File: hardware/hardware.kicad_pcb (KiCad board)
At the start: 2 copper layers, 91.4 x 91.4 mm, 104 parts, among them J1 DB25_Female, J2 USB_B_Micro, J3 RJ45_Bel_SI-60062-F-68net, J4 Conn_01x02_Male, J5 Conn_01x02_Male, U1 MIC5319, U11 ENC28J60x-SO, U12 74LVC14, U2 74LVTH126, U3 74LVTH126, U4 LM1117-ADJ, U5 74LVTH126, U6 74LVTH126, U7 STM32F072R8Tx, U8 74LVC245, Y1 8MHz, Y2 25MHz

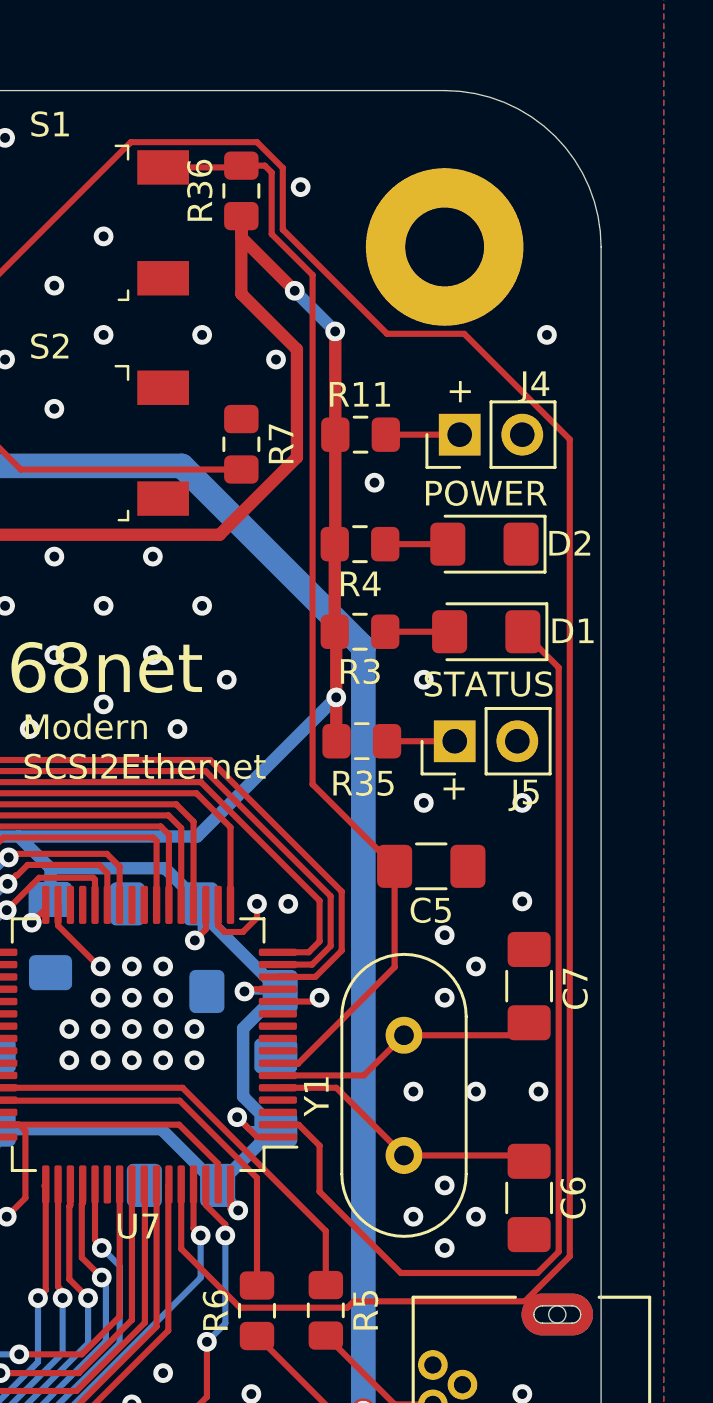
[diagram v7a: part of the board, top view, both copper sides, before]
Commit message: fix: wrong pins on LEDs connectors
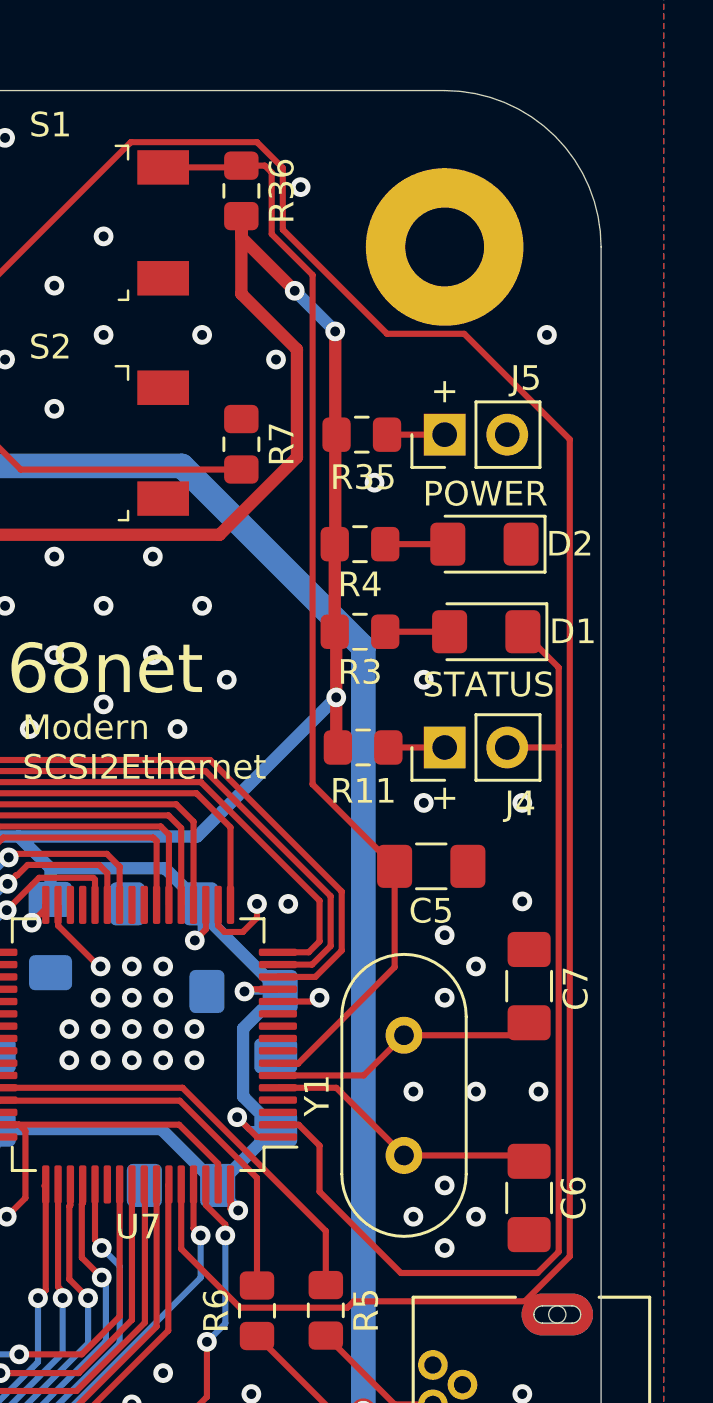
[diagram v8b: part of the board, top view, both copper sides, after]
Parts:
- moved J4 12.7 mm to (105.4, 47.0)
- moved R11 12.7 mm to (102.1, 47.0)
- moved J5 12.5 mm to (105.4, 34.3)
- moved R35 12.4 mm to (102.0, 34.3)
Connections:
- J4 pad 2: GND -> /STATUS_LED
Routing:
- net /STATUS_LED: track 41.1 -> 43.2 mm
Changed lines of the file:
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@@
     (thickness 1.6)
     (drawings 18)
-    (tracks 1581)
+    (tracks 1585)
     (zones 0)
     (modules 104)
@@
   )
   (setup
-    (last_trace_width 0.5)
+    (last_trace_width 0.25)
     (user_trace_width 0.25)
     (user_trace_width 0.5)
@@
     (tags "resistor handsolder")
     (attr smd)
-    (fp_text reference R36 (at 0 -1.65 90) (layer F.SilkS)
+    (fp_text reference R36 (at 0 1.651 90) (layer F.SilkS)
       (effects (font (size 1 1) (thickness 0.15)))
     )
@@
   )
   (module Resistor_SMD:R_0805_2012Metric_Pad1.15x1.40mm_HandSolder (layer F.Cu)
-    (at 102.045 46.736 180)
+    (at 102.045 34.29 180)
     (descr "Resistor SMD 0805 (2012 Metric), square (rectangular) end terminal, IPC_7351 nominal with elongated pad for handsoldering. (Body size source: https://docs.google.com/spreadsheets/d/1BsfQQcO9C6DZCsRaXUlFlo91Tg2WpOkGARC1WS5S8t0/edit?usp=sharing), generated with kicad-footprint-generator")
     (tags "resistor handsolder")
@@
   )
   (module Resistor_SMD:R_0805_2012Metric_Pad1.15x1.40mm_HandSolder (layer F.Cu)
-    (at 101.995 34.29 180)
+    (at 102.099 46.99 180)
     (descr "Resistor SMD 0805 (2012 Metric), square (rectangular) end terminal, IPC_7351 nominal with elongated pad for handsoldering. (Body size source: https://docs.google.com/spreadsheets/d/1BsfQQcO9C6DZCsRaXUlFlo91Tg2WpOkGARC1WS5S8t0/edit?usp=sharing), generated with kicad-footprint-generator")
     (tags "resistor handsolder")
     (attr smd)
-    (fp_text reference R11 (at 0.025 1.6) (layer F.SilkS)
+    (fp_text reference R11 (at -0.009 -1.778) (layer F.SilkS)
       (effects (font (size 1 1) (thickness 0.15)))
     )
@@
   )
   (module Connector_PinHeader_2.54mm:PinHeader_1x02_P2.54mm_Vertical (layer F.Cu)
-    (at 105.82 46.736 90)
+    (at 105.41 34.29 90)
     (descr "Through hole straight pin header, 1x02, 2.54mm pitch, single row")
     (tags "Through hole pin header THT 1x02 2.54mm single row")
-    (fp_text reference J5 (at -2.1 2.892 180) (layer F.SilkS)
+    (fp_text reference J5 (at 2.286 3.302 180) (layer F.SilkS)
       (effects (font (size 1 1) (thickness 0.15)))
     )
@@
   )
   (module Connector_PinHeader_2.54mm:PinHeader_1x02_P2.54mm_Vertical (layer F.Cu)
-    (at 106.02 34.29 90)
+    (at 105.41 46.99 90)
     (descr "Through hole straight pin header, 1x02, 2.54mm pitch, single row")
     (tags "Through hole pin header THT 1x02 2.54mm single row")
-    (fp_text reference J4 (at 2.032 3.073 180) (layer F.SilkS)
+    (fp_text reference J4 (at -2.286 3.073 180) (layer F.SilkS)
       (effects (font (size 1 1) (thickness 0.15)))
     )
@@
     )
     (pad 2 thru_hole oval (at 0 2.54 90) (size 1.7 1.7) (drill 1) (layers *.Cu *.Mask)
-      (net 1 GND))
+      (net 15 /STATUS_LED))
     (pad 1 thru_hole rect (at 0 0 90) (size 1.7 1.7) (drill 1) (layers *.Cu *.Mask)
       (net 111 "Net-(J4-Pad1)"))
@@
     )
   )
-  (gr_text + (at 106.045 32.512) (layer F.SilkS)
+  (gr_text + (at 105.41 32.512) (layer F.SilkS)
     (effects (font (size 1 1) (thickness 0.2)))
   )
-  (gr_text + (at 105.791 48.641) (layer F.SilkS)
+  (gr_text + (at 105.41 49.022) (layer F.SilkS)
     (effects (font (size 1 1) (thickness 0.2)))
   )
@@
   (segment (start 100.33 63.155298) (end 100.33 65.024) (width 0.25) (layer F.Cu) (net 15))
   (segment (start 100.33 65.024) (end 103.632 68.326) (width 0.25) (layer F.Cu) (net 15))
-  (segment (start 110.03901 67.46618) (end 110.03901 43.74501) (width 0.25) (layer F.Cu) (net 15))
   (segment (start 110.03901 43.74501) (end 108.585 42.291) (width 0.25) (layer F.Cu) (net 15))
   (segment (start 109.17919 68.326) (end 110.03901 67.46618) (width 0.25) (layer F.Cu) (net 15))
   (segment (start 103.632 68.326) (end 109.17919 68.326) (width 0.25) (layer F.Cu) (net 15))
+  (segment (start 107.95 46.99) (end 109.982 46.99) (width 0.25) (layer F.Cu) (net 15))
+  (segment (start 110.03901 46.93299) (end 110.03901 43.74501) (width 0.25) (layer F.Cu) (net 15))
+  (segment (start 109.982 46.99) (end 110.03901 46.93299) (width 0.25) (layer F.Cu) (net 15))
+  (segment (start 110.03901 67.46618) (end 110.03901 46.93299) (width 0.25) (layer F.Cu) (net 15))
   (segment (start 102.997 38.735) (end 105.537 38.735) (width 0.25) (layer F.Cu) (net 16))
   (segment (start 55.75 50.8) (end 54.61 51.94) (width 0.25) (layer F.Cu) (net 17))
@@
   (segment (start 50.238 26.381) (end 50.339 26.482) (width 0.5) (layer F.Cu) (net 110))
   (segment (start 50.238 24.13) (end 50.238 26.381) (width 0.5) (layer F.Cu) (net 110))
-  (segment (start 103.02 34.29) (end 106.02 34.29) (width 0.25) (layer F.Cu) (net 111))
-  (segment (start 105.72 46.52) (end 105.82 46.42) (width 0.25) (layer F.Cu) (net 112))
-  (segment (start 103.07 46.736) (end 105.82 46.736) (width 0.25) (layer F.Cu) (net 112))
+  (segment (start 105.156 46.736) (end 105.41 46.99) (width 0.25) (layer F.Cu) (net 111))
+  (segment (start 103.124 46.99) (end 105.41 46.99) (width 0.25) (layer F.Cu) (net 111))
+  (segment (start 105.156 34.544) (end 105.41 34.29) (width 0.25) (layer F.Cu) (net 112))
+  (segment (start 103.07 34.29) (end 105.41 34.29) (width 0.25) (layer F.Cu) (net 112))
   (zone (net 1) (net_name GND) (layer F.Cu) (hatch edge 0.508)
     (connect_pads (clearance 0.508))
